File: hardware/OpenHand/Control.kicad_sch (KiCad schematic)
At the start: 0 parts

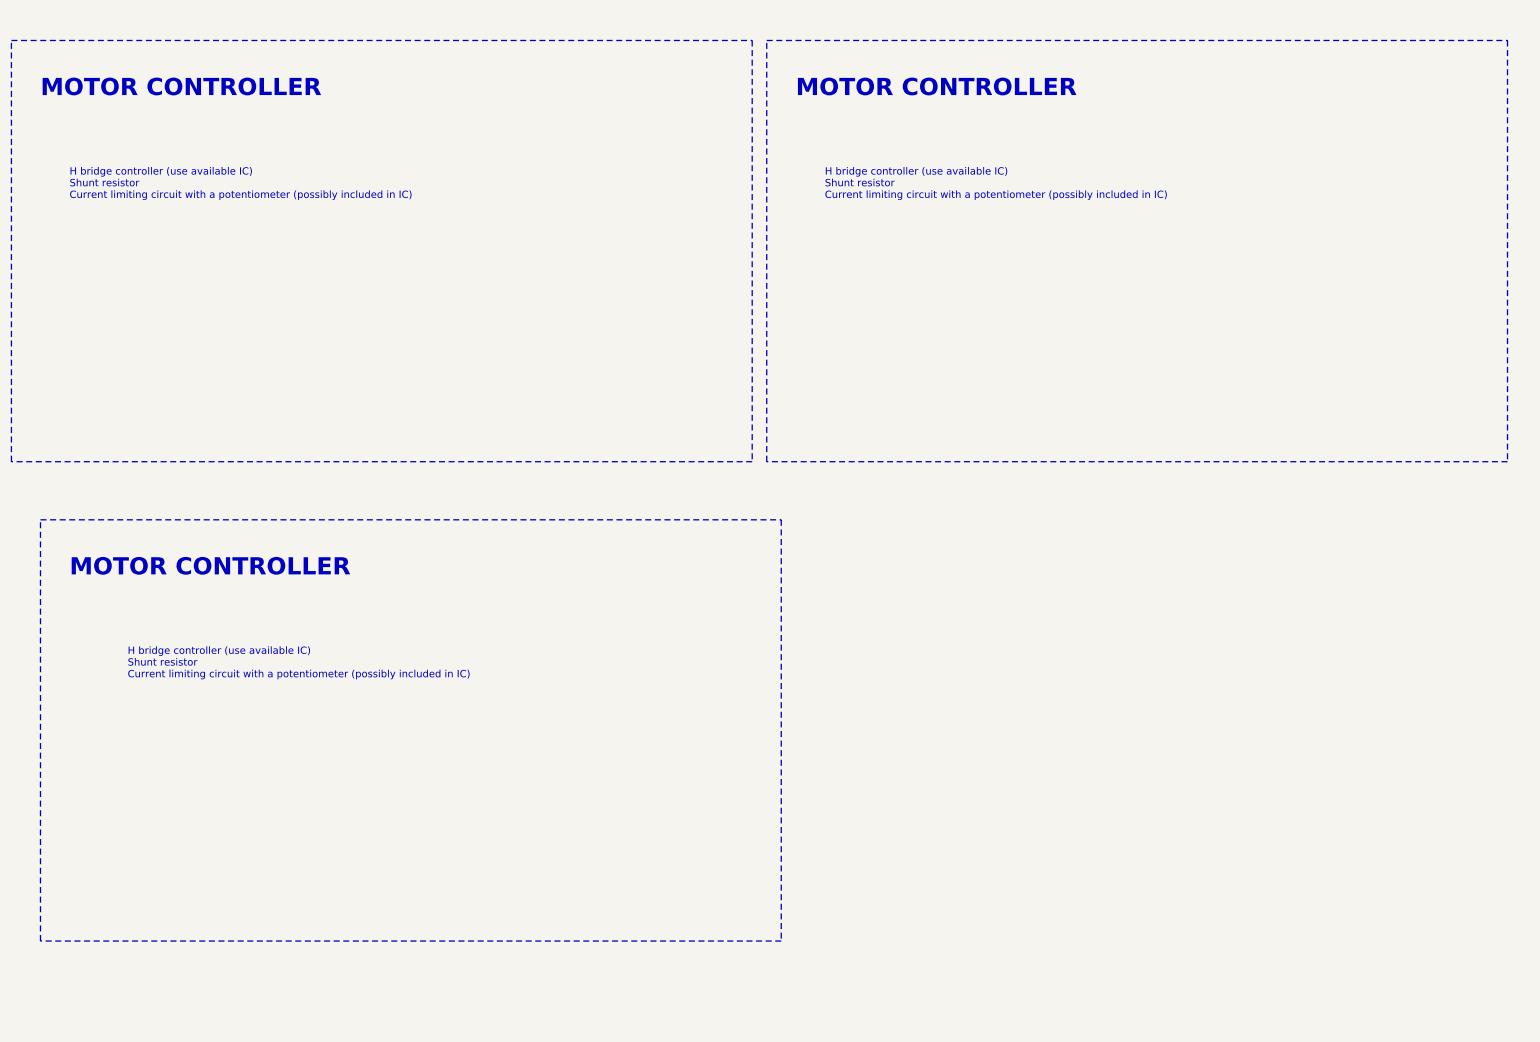
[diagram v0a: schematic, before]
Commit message: Started adding ICs to schematic
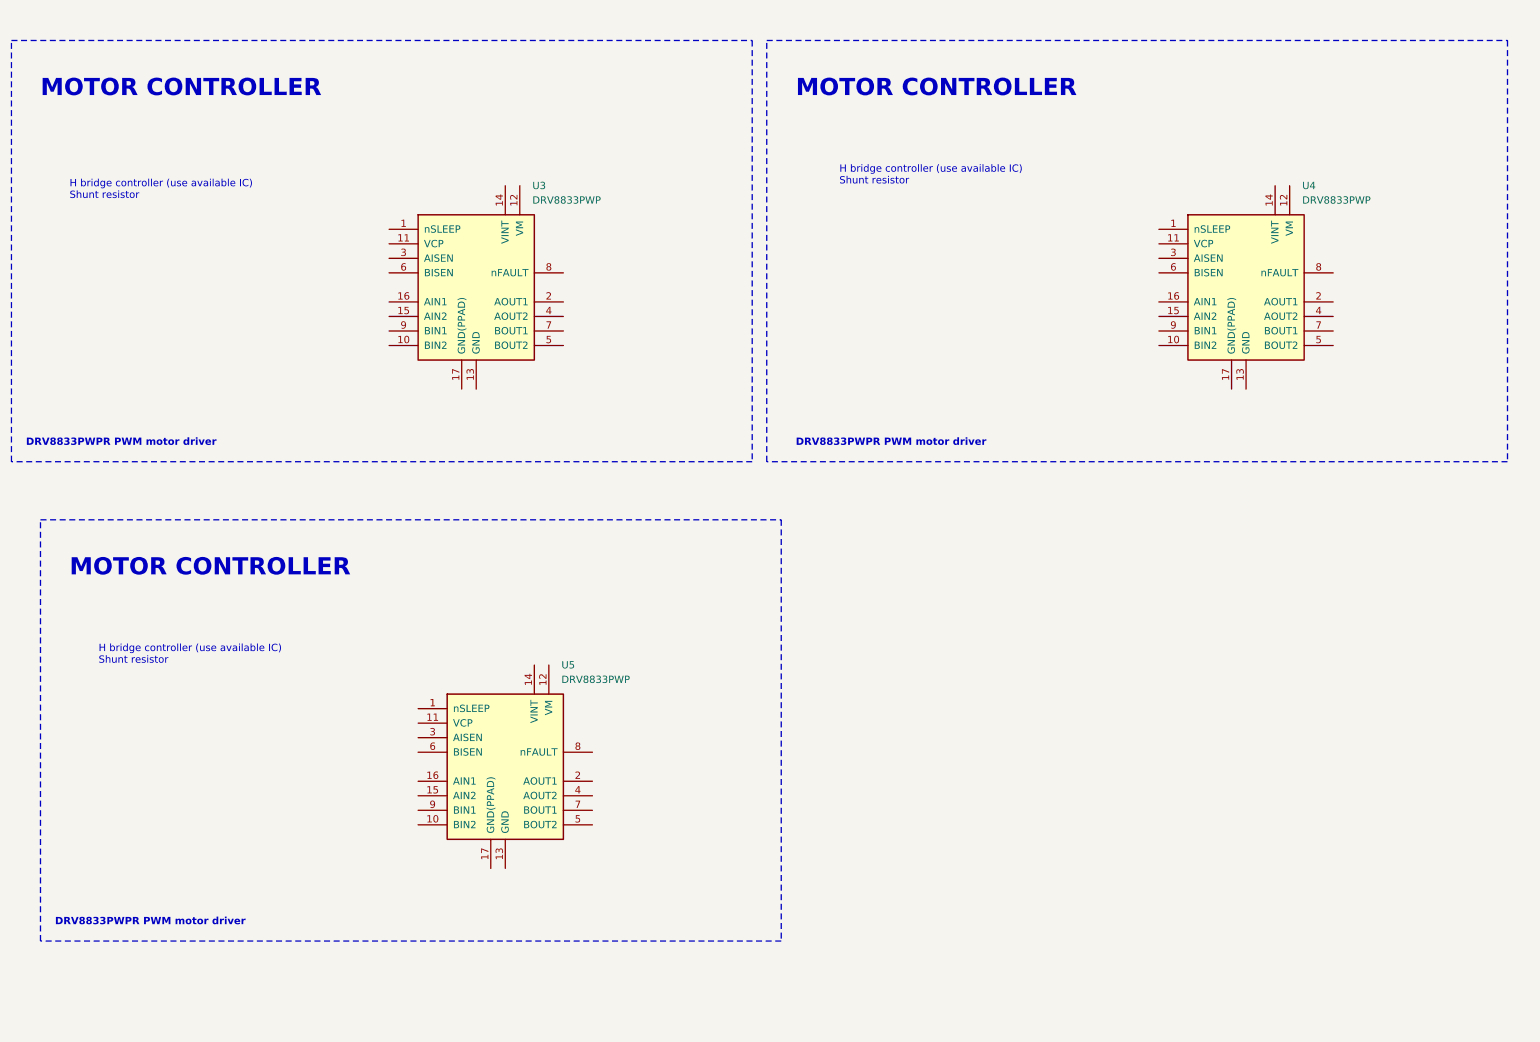
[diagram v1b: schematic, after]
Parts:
- added U3, U4, U5: DRV8833PWP, Package_SO:HTSSOP-16-1EP_4.4x5mm_P0.65mm_EP3.4x5mm_Mask2.46x2.31mm_ThermalVias, symbol Driver_Motor:DRV8833PWP
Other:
- note added: "DRV8833PWPR PWM motor driver"
- note added: "H bridge controller (use available IC) Shunt resistor"
- note removed: "H bridge controller (use available IC) Shunt resistor Current limiting circuit with a potentiometer (possibly included in IC)"
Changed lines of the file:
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@@
     (fill (type none))
   )
-  (text "H bridge controller (use available IC)\nShunt resistor\nCurrent limiting circuit with a potentiometer (possibly included in IC)"
-    (at 35.56 134.62 0)
+  (text "H bridge controller (use available IC)\nShunt resistor"
+    (at 30.48 132.08 0)
     (effects (font (size 1.27 1.27)) (justify left bottom))
   )
@@
     (effects (font (size 3 3) (thickness 0.6) bold) (justify left bottom))
   )
-  (text "H bridge controller (use available IC)\nShunt resistor\nCurrent limiting circuit with a potentiometer (possibly included in IC)"
+  (text "DRV8833PWPR PWM motor driver" (at 22.86 177.8 0)
+    (effects (font (size 1.27 1.27) (thickness 0.254) bold) (justify left bottom) (href "https://www.lcsc.com/product-detail/Motor-Driver-ICs_Texas-Instruments-DRV8833PWPR_C50506.html"))
+  )
+  (text "H bridge controller (use available IC)\nShunt resistor"
     (at 25.4 50.8 0)
     (effects (font (size 1.27 1.27)) (justify left bottom))
@@
     (effects (font (size 3 3) (thickness 0.6) bold) (justify left bottom))
   )
-  (text "H bridge controller (use available IC)\nShunt resistor\nCurrent limiting circuit with a potentiometer (possibly included in IC)"
-    (at 157.48 50.8 0)
+  (text "DRV8833PWPR PWM motor driver" (at 17.78 93.98 0)
+    (effects (font (size 1.27 1.27) (thickness 0.254) bold) (justify left bottom) (href "https://www.lcsc.com/product-detail/Motor-Driver-ICs_Texas-Instruments-DRV8833PWPR_C50506.html"))
+  )
+  (text "DRV8833PWPR PWM motor driver" (at 152.4 93.98 0)
+    (effects (font (size 1.27 1.27) (thickness 0.254) bold) (justify left bottom) (href "https://www.lcsc.com/product-detail/Motor-Driver-ICs_Texas-Instruments-DRV8833PWPR_C50506.html"))
+  )
+  (text "H bridge controller (use available IC)\nShunt resistor"
+    (at 160.02 48.26 0)
     (effects (font (size 1.27 1.27)) (justify left bottom))
   )
+  (symbol (lib_id "Driver_Motor:DRV8833PWP") (at 101.6 149.86 0) (unit 1)
+    (in_bom yes) (on_board yes) (dnp no) (fields_autoplaced)
+    (property "Reference" "U5" (at 111.4141 132.08 0)
+      (effects (font (size 1.27 1.27)) (justify left))
+    )
+    (property "Value" "DRV8833PWP" (at 111.4141 134.62 0)
+      (effects (font (size 1.27 1.27)) (justify left))
+    )
+    (property "Footprint" "Package_SO:HTSSOP-16-1EP_4.4x5mm_P0.65mm_EP3.4x5mm_Mask2.46x2.31mm_ThermalVias" (at 113.03 138.43 0)
+      (effects (font (size 1.27 1.27)) (justify left) hide)
+    )
+    (property "Datasheet" "http://www.ti.com/lit/ds/symlink/drv8833.pdf" (at 97.79 135.89 0)
+      (effects (font (size 1.27 1.27)) hide)
+    )
+    (pin "1")
+    (pin "10")
+    (pin "11")
+    (pin "12")
+    (pin "13")
+    (pin "14")
+    (pin "15")
+    (pin "16")
+    (pin "17")
+    (pin "2")
+    (pin "3")
+    (pin "4")
+    (pin "5")
+    (pin "6")
+    (pin "7")
+    (pin "8")
+    (pin "9")
+    (instances
+      (project "OpenHand"
+        (path "/f1fbd835-8408-4592-854c-2fbec9d052ec/20793231-6e6d-417f-8f1f-2d40174b5a27"
+          (reference "U5") (unit 1)
+        )
+      )
+    )
+  )
+  (symbol (lib_id "Driver_Motor:DRV8833PWP") (at 96.52 66.04 0) (unit 1)
+    (in_bom yes) (on_board yes) (dnp no) (fields_autoplaced)
+    (property "Reference" "U3" (at 106.3341 48.26 0)
+      (effects (font (size 1.27 1.27)) (justify left))
+    )
+    (property "Value" "DRV8833PWP" (at 106.3341 50.8 0)
+      (effects (font (size 1.27 1.27)) (justify left))
+    )
+    (property "Footprint" "Package_SO:HTSSOP-16-1EP_4.4x5mm_P0.65mm_EP3.4x5mm_Mask2.46x2.31mm_ThermalVias" (at 107.95 54.61 0)
+      (effects (font (size 1.27 1.27)) (justify left) hide)
+    )
+    (property "Datasheet" "http://www.ti.com/lit/ds/symlink/drv8833.pdf" (at 92.71 52.07 0)
+      (effects (font (size 1.27 1.27)) hide)
+    )
+    (pin "1")
+    (pin "10")
+    (pin "11")
+    (pin "12")
+    (pin "13")
+    (pin "14")
+    (pin "15")
+    (pin "16")
+    (pin "17")
+    (pin "2")
+    (pin "3")
+    (pin "4")
+    (pin "5")
+    (pin "6")
+    (pin "7")
+    (pin "8")
+    (pin "9")
+    (instances
+      (project "OpenHand"
+        (path "/f1fbd835-8408-4592-854c-2fbec9d052ec/20793231-6e6d-417f-8f1f-2d40174b5a27"
+          (reference "U3") (unit 1)
+        )
+      )
+    )
+  )
+  (symbol (lib_id "Driver_Motor:DRV8833PWP") (at 231.14 66.04 0) (unit 1)
+    (in_bom yes) (on_board yes) (dnp no) (fields_autoplaced)
+    (property "Reference" "U4" (at 240.9541 48.26 0)
+      (effects (font (size 1.27 1.27)) (justify left))
+    )
+    (property "Value" "DRV8833PWP" (at 240.9541 50.8 0)
+      (effects (font (size 1.27 1.27)) (justify left))
+    )
+    (property "Footprint" "Package_SO:HTSSOP-16-1EP_4.4x5mm_P0.65mm_EP3.4x5mm_Mask2.46x2.31mm_ThermalVias" (at 242.57 54.61 0)
+      (effects (font (size 1.27 1.27)) (justify left) hide)
+    )
+    (property "Datasheet" "http://www.ti.com/lit/ds/symlink/drv8833.pdf" (at 227.33 52.07 0)
+      (effects (font (size 1.27 1.27)) hide)
+    )
+    (pin "1")
+    (pin "10")
+    (pin "11")
+    (pin "12")
+    (pin "13")
+    (pin "14")
+    (pin "15")
+    (pin "16")
+    (pin "17")
+    (pin "2")
+    (pin "3")
+    (pin "4")
+    (pin "5")
+    (pin "6")
+    (pin "7")
+    (pin "8")
+    (pin "9")
+    (instances
+      (project "OpenHand"
+        (path "/f1fbd835-8408-4592-854c-2fbec9d052ec/20793231-6e6d-417f-8f1f-2d40174b5a27"
+          (reference "U4") (unit 1)
+        )
+      )
+    )
+  )
 )

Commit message: Update schematic
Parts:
- removed U3, U4: DRV8833PWP, Package_SO:HTSSOP-16-1EP_4.4x5mm_P0.65mm_EP3.4x5mm_Mask2.46x2.31mm_ThermalVias, symbol Driver_Motor:DRV8833PWP
- added C10, C4, C5: 2u2, symbol Device:C
- added C11, C6, C7: 10n, symbol Device:C
- added C12, C8, C9: 10u, symbol Device:C
- added R7, R8, R9: 0R200, symbol Device:R
- added U5, U6: DRV8833PWP, Package_SO:HTSSOP-16-1EP_4.4x5mm_P0.65mm_EP3.4x5mm_Mask2.46x2.31mm_ThermalVias, symbol Driver_Motor:DRV8833PWP
- renumbered U5 to U7
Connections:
- net MOTOR_3_EN: now reaches U7.1 (nSLEEP)
- net MOTOR_3_IN2: now reaches U7.10 (BIN2)
- net MOTOR_3_IN2: now also U7.15 (AIN2)
- net at U7.11 (VCP): now also C11.2
- net +5V: now reaches U7.12 (VM)
- net +5V: now also C11.1, C12.1, C6.1, C7.1, C8.1, C9.1, U5.12 (VM), U6.12 (VM)
- net Earth: now reaches U7.13 (GND)
- net Earth: now also U7.17 (GND(PPAD)), C10.1, C12.2, C4.1, C5.1, C8.2, C9.2, R7.1, R8.1, R9.1, U5.13 (GND), U5.17 (GND(PPAD)), U6.13 (GND), U6.17 (GND(PPAD))
- net at U7.14 (VINT): now also C10.2
- net MOTOR_3_IN1: now reaches U7.16 (AIN1)
- net MOTOR_3_IN1: now also U7.9 (BIN1)
- net MOTOR_3_P: now reaches U7.2 (AOUT1)
- net MOTOR_3_P: now also U7.7 (BOUT1)
- net at U7.3 (AISEN): now also U7.6 (BISEN), R9.2
- net MOTOR_3_N: now reaches U7.4 (AOUT2)
- net MOTOR_3_N: now also U7.5 (BOUT2)
- net MOTOR_3_FAULT: now reaches U7.8 (nFAULT)
- new net: C7.2, U6.11 (VCP)
- new net: C5.2, U6.14 (VINT)
- new net: R8.2, U6.3 (AISEN), U6.6 (BISEN)
- new net: C6.2, U5.11 (VCP)
- new net: C4.2, U5.14 (VINT)
- new net: R7.2, U5.3 (AISEN), U5.6 (BISEN)
- new net MOTOR_1_EN: U5.1 (nSLEEP)
- new net MOTOR_1_FAULT: U5.8 (nFAULT)
- new net MOTOR_1_IN1: U5.16 (AIN1), U5.9 (BIN1)
- new net MOTOR_1_IN2: U5.10 (BIN2), U5.15 (AIN2)
- new net MOTOR_1_N: U5.4 (AOUT2), U5.5 (BOUT2)
- new net MOTOR_1_P: U5.2 (AOUT1), U5.7 (BOUT1)
- new net MOTOR_2_EN: U6.1 (nSLEEP)
- new net MOTOR_2_FAULT: U6.8 (nFAULT)
- new net MOTOR_2_IN1: U6.16 (AIN1), U6.9 (BIN1)
- new net MOTOR_2_IN2: U6.10 (BIN2), U6.15 (AIN2)
- new net MOTOR_2_N: U6.4 (AOUT2), U6.5 (BOUT2)
- new net MOTOR_2_P: U6.2 (AOUT1), U6.7 (BOUT1)
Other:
- note removed: "H bridge controller (use available IC) Shunt resistor"
- moved on the sheet: U7

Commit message: working on schematics
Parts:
- C10, C11, C12, C4, C5, C6, C7, C8, C9: footprint (none) -> Capacitor_SMD:C_1206_3216Metric
- renumbered R7 to R13, R8 to R14, R9 to R15, U5 to U7, U6 to U8, U7 to U9
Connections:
- net MOTOR_1_IN1 renamed MOTOR_1_UC1
- net MOTOR_1_IN2 renamed MOTOR_1_UC2
- net MOTOR_2_IN1 renamed MOTOR_2_UC1
- net MOTOR_2_IN2 renamed MOTOR_2_UC2
- net MOTOR_3_IN1 renamed MOTOR_3_UC1
- net MOTOR_3_IN2 renamed MOTOR_3_UC2
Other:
- note added: "TODO: put some short description of circuit and components here, how it operates..."
- title: (none) -> OpenHand prosthetic hand controller project

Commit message: Update ME, SCH and documentation a bit
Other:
- note added: "Low current vibrating motors for haptic feedback"
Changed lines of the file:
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@@
     (fill (type none))
+  )
+  (text "Low current vibrating motors for haptic feedback" (at 165.1 125.73 0)
+    (effects (font (size 1.27 1.27)) (justify left bottom))
   )
   (text "TODO: put some short description of circuit \nand components here, how it operates..."

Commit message: Minor updates to schm
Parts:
- added C12: 2u2, Capacitor_SMD:C_1206_3216Metric, symbol Device:C
- added C14: 10n, Capacitor_SMD:C_1206_3216Metric, symbol Device:C
- added C16: 10u, Capacitor_SMD:C_1206_3216Metric, symbol Device:C
- added R19, R21: 0R200, symbol Device:R
- added U7: DRV8833PWP, Package_SO:HTSSOP-16-1EP_4.4x5mm_P0.65mm_EP3.4x5mm_Mask2.46x2.31mm_ThermalVias, symbol Driver_Motor:DRV8833PWP
- renumbered C9 to C10, C10 to C11, C11 to C13, C12 to C15, C4 to C5, C5 to C6, C6 to C7, C7 to C8, C8 to C9, R13 to R17, R14 to R18, R15 to R20, U7 to U4, U8 to U5, U9 to U6
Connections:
- net +5V: now also C14.1, C16.1, U7.12 (VM)
- net Earth: now also C12.1, C16.2, R19.1, R21.1, U7.13 (GND), U7.17 (GND(PPAD))
- new net: C14.2, U7.11 (VCP)
- new net: C12.2, U7.14 (VINT)
- new net: R19.2, U7.3 (AISEN)
- new net: R21.2, U7.6 (BISEN)
- new net FDBK_MOTOR_1_N: U7.4 (AOUT2)
- new net FDBK_MOTOR_1_P: U7.2 (AOUT1)
- new net FDBK_MOTOR_1_UC1: U7.16 (AIN1)
- new net FDBK_MOTOR_1_UC2: U7.15 (AIN2)
- new net FDBK_MOTOR_2_N: U7.5 (BOUT2)
- new net FDBK_MOTOR_2_P: U7.7 (BOUT1)
- new net FDBK_MOTOR_2_UC1: U7.9 (BIN1)
- new net FDBK_MOTOR_2_UC2: U7.10 (BIN2)
- new net FDBK_MOTOR_EN: U7.1 (nSLEEP)
- new net FDBK_MOTOR_FAULT: U7.8 (nFAULT)
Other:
- note added: "HAPTIC FEEDBACK MOTOR CONTROLLER"
- note added: "TODO: Change sense resistors for much lower current. Find out what current are haptic vibrating motors"
- note added: "TODO: put some short description of circuit and components here, how it operates... Sense resistro and current limiting, en and fault signals, PWM configuration... Doubling up the channels for more current"
- note removed: "Low current vibrating motors for haptic feedback"
- note removed: "TODO: put some short description of circuit and components here, how it operates..."
- moved on the sheet: C11, C13, C15, R20, U6

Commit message: Update schematic a bit
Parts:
- R19, R21: value 0R200 -> 4R7
- renumbered U4 to U6, U5 to U7, U6 to U8, U7 to U9
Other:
- note added: "Cutoff current 1A RSENSE = 0.2 V / 1 A = 0.2 Ω"
- note added: "Cutoff current ~42.5mA RSENSE = 0.2 V / 0.0425 A = ~4.7 Ω"
- note added: "Using PWM and GPIO signals on pins xIN1 and xIN2, we can control the speed (current) and direction of connected DC motors. Looking at the datasheet, we can use xIN1 as PWM for speed, and xIN2 as direction input (HIGH for reverse, LOW for forward). PWM frequency should be 50kHz. When the voltage on pin xISEN exceeds VTRIP (0.2 V), current regulation is activated. The RISENSE resistor should be siz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"
- note removed: "TODO: Change sense resistors for much lower current. Find out what current are haptic vibrating motors"
- note removed: "TODO: put some short description of circuit and components here, how it operates... Sense resistro and current limiting, en and fault signals, PWM configuration... Doubling up the channels for more current"
